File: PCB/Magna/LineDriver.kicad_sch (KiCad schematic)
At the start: 38 parts, among them J1301 PSG01550, U1301 NE5532, U1302 NE5532, U1303 NE5532

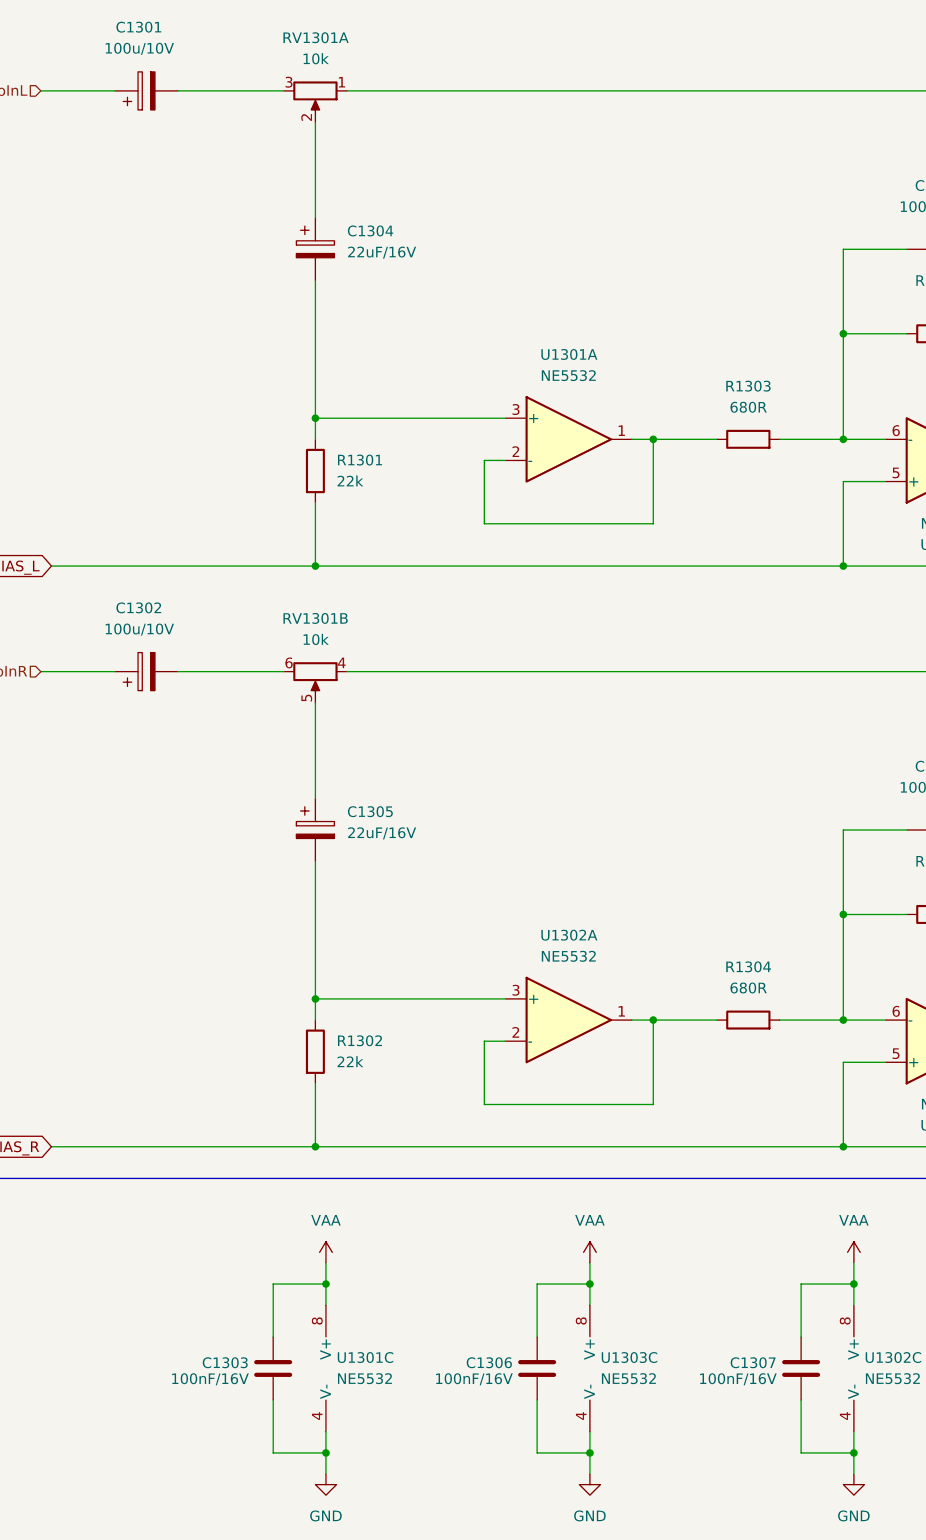
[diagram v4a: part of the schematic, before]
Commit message: Add even more component footprints and partnumbers
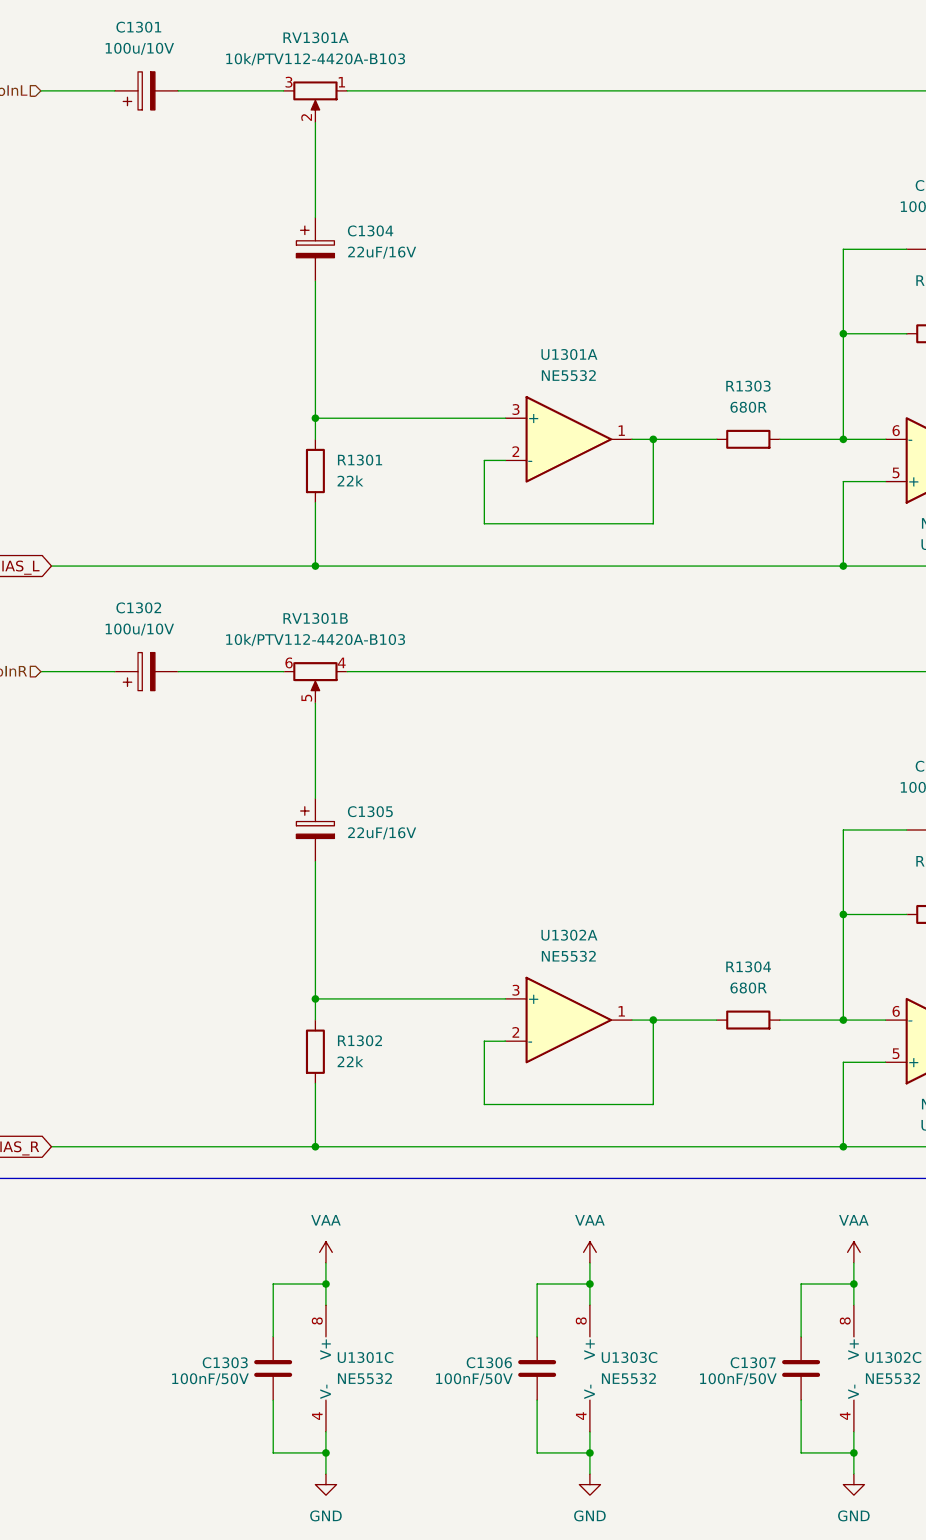
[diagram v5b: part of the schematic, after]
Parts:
- C1303, C1306, C1307: value 100nF/16V -> 100nF/50V; footprint Capacitor_SMD:C_0805_2012Metric -> Capacitor_SMD:C_0805_2012Metric_Pad1.18x1.45mm_HandSolder; LCSC C218638 -> C49678
- C1308, C1309, C1312, C1313: footprint Capacitor_SMD:C_0805_2012Metric -> Capacitor_SMD:C_0805_2012Metric_Pad1.18x1.45mm_HandSolder
- J1301: footprint (none) -> Skrooter_footprints:psg01550
- R1301, R1302, R1307, R1308, R1317, R1318: footprint Resistor_SMD:R_0805_2012Metric -> Resistor_SMD:R_0805_2012Metric_Pad1.20x1.40mm_HandSolder
- RV1301: value 10k -> 10k/PTV112-4420A-B103; footprint (none) -> Skrooter_footprints:Potentiometer_Bourns_PTV09A-1_Dual_Vertical
- U1301, U1302, U1303: footprint (none) -> Package_SO:SOIC-8_3.9x4.9mm_P1.27mm
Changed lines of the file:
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@@
       (effects (font (size 1.27 1.27)))
     )
-    (property "Value" "10k" (at 58.42 20.32 90)
-      (effects (font (size 1.27 1.27)))
-    )
-    (property "Footprint" "" (at 58.42 24.13 0)
+    (property "Value" "10k/PTV112-4420A-B103" (at 58.42 20.32 90)
+      (effects (font (size 1.27 1.27)))
+    )
+    (property "Footprint" "Skrooter_footprints:Potentiometer_Bourns_PTV09A-1_Dual_Vertical" (at 58.42 24.13 0)
       (effects (font (size 1.27 1.27)) hide)
     )
@@
       (effects (font (size 1.27 1.27)))
     )
-    (property "Footprint" "" (at 200.66 115.57 0)
+    (property "Footprint" "Package_SO:SOIC-8_3.9x4.9mm_P1.27mm" (at 200.66 115.57 0)
       (effects (font (size 1.27 1.27)) hide)
     )
@@
       (effects (font (size 1.27 1.27)) (justify left))
     )
-    (property "Value" "100nF/16V" (at 82.169 179.0773 0)
-      (effects (font (size 1.27 1.27)) (justify left))
-    )
-    (property "Footprint" "Capacitor_SMD:C_0805_2012Metric" (at 84.1248 181.61 0)
+    (property "Value" "100nF/50V" (at 82.169 179.0773 0)
+      (effects (font (size 1.27 1.27)) (justify left))
+    )
+    (property "Footprint" "Capacitor_SMD:C_0805_2012Metric_Pad1.18x1.45mm_HandSolder" (at 84.1248 181.61 0)
       (effects (font (size 1.27 1.27)) hide)
     )
@@
       (effects (font (size 1.27 1.27)) hide)
     )
-    (property "LCSC" "C218638" (at 85.09 177.8 0)
+    (property "LCSC" "C49678" (at 85.09 177.8 0)
       (effects (font (size 1.27 1.27)) hide)
     )
@@
       (effects (font (size 1.27 1.27)))
     )
-    (property "Footprint" "" (at 134.62 68.58 0)
+    (property "Footprint" "Package_SO:SOIC-8_3.9x4.9mm_P1.27mm" (at 134.62 68.58 0)
       (effects (font (size 1.27 1.27)) hide)
     )
@@
       (effects (font (size 1.27 1.27)))
     )
-    (property "Footprint" "" (at 200.66 45.72 0)
+    (property "Footprint" "Package_SO:SOIC-8_3.9x4.9mm_P1.27mm" (at 200.66 45.72 0)
       (effects (font (size 1.27 1.27)) hide)
     )
@@
       (effects (font (size 1.27 1.27)) (justify left))
     )
-    (property "Footprint" "" (at 265.43 91.44 0)
+    (property "Footprint" "Skrooter_footprints:psg01550" (at 265.43 91.44 0)
       (effects (font (size 1.27 1.27)) hide)
     )
@@
       (effects (font (size 1.27 1.27)))
     )
-    (property "Footprint" "Capacitor_SMD:C_0805_2012Metric" (at 137.16 42.2148 0)
+    (property "Footprint" "Capacitor_SMD:C_0805_2012Metric_Pad1.18x1.45mm_HandSolder" (at 137.16 42.2148 0)
       (effects (font (size 1.27 1.27)) hide)
     )
@@
       (effects (font (size 1.27 1.27)) (justify left))
     )
-    (property "Footprint" "Resistor_SMD:R_0805_2012Metric" (at 163.322 74.93 90)
+    (property "Footprint" "Resistor_SMD:R_0805_2012Metric_Pad1.20x1.40mm_HandSolder" (at 163.322 74.93 90)
       (effects (font (size 1.27 1.27)) hide)
     )
@@
       (effects (font (size 1.27 1.27)) (justify left))
     )
-    (property "Footprint" "Resistor_SMD:R_0805_2012Metric" (at 56.642 139.7 90)
+    (property "Footprint" "Resistor_SMD:R_0805_2012Metric_Pad1.20x1.40mm_HandSolder" (at 56.642 139.7 90)
       (effects (font (size 1.27 1.27)) hide)
     )
@@
       (effects (font (size 1.27 1.27)))
     )
-    (property "Footprint" "" (at 134.62 138.43 0)
+    (property "Footprint" "Package_SO:SOIC-8_3.9x4.9mm_P1.27mm" (at 134.62 138.43 0)
       (effects (font (size 1.27 1.27)) hide)
     )
@@
       (effects (font (size 1.27 1.27)) (justify left))
     )
-    (property "Footprint" "Resistor_SMD:R_0805_2012Metric" (at 247.142 124.46 90)
+    (property "Footprint" "Resistor_SMD:R_0805_2012Metric_Pad1.20x1.40mm_HandSolder" (at 247.142 124.46 90)
       (effects (font (size 1.27 1.27)) hide)
     )
@@
       (effects (font (size 1.27 1.27)))
     )
-    (property "Footprint" "" (at 88.9 135.89 0)
+    (property "Footprint" "Package_SO:SOIC-8_3.9x4.9mm_P1.27mm" (at 88.9 135.89 0)
       (effects (font (size 1.27 1.27)) hide)
     )
@@
       (effects (font (size 1.27 1.27)))
     )
-    (property "Footprint" "Capacitor_SMD:C_0805_2012Metric" (at 137.16 112.0648 0)
+    (property "Footprint" "Capacitor_SMD:C_0805_2012Metric_Pad1.18x1.45mm_HandSolder" (at 137.16 112.0648 0)
       (effects (font (size 1.27 1.27)) hide)
     )
@@
       (effects (font (size 1.27 1.27)) (justify left))
     )
-    (property "Footprint" "" (at 62.23 177.8 0)
+    (property "Footprint" "Package_SO:SOIC-8_3.9x4.9mm_P1.27mm" (at 62.23 177.8 0)
       (effects (font (size 1.27 1.27)) hide)
     )
@@
       (effects (font (size 1.27 1.27)) (justify left))
     )
-    (property "Footprint" "Resistor_SMD:R_0805_2012Metric" (at 247.142 54.61 90)
+    (property "Footprint" "Resistor_SMD:R_0805_2012Metric_Pad1.20x1.40mm_HandSolder" (at 247.142 54.61 90)
       (effects (font (size 1.27 1.27)) hide)
     )
@@
       (effects (font (size 1.27 1.27)))
     )
-    (property "Footprint" "Capacitor_SMD:C_0805_2012Metric" (at 204.47 34.5948 0)
+    (property "Footprint" "Capacitor_SMD:C_0805_2012Metric_Pad1.18x1.45mm_HandSolder" (at 204.47 34.5948 0)
       (effects (font (size 1.27 1.27)) hide)
     )
@@
       (effects (font (size 1.27 1.27)) (justify left))
     )
-    (property "Footprint" "" (at 125.73 177.8 0)
+    (property "Footprint" "Package_SO:SOIC-8_3.9x4.9mm_P1.27mm" (at 125.73 177.8 0)
       (effects (font (size 1.27 1.27)) hide)
     )
@@
       (effects (font (size 1.27 1.27)) (justify left))
     )
-    (property "Footprint" "Resistor_SMD:R_0805_2012Metric" (at 56.642 69.85 90)
+    (property "Footprint" "Resistor_SMD:R_0805_2012Metric_Pad1.20x1.40mm_HandSolder" (at 56.642 69.85 90)
       (effects (font (size 1.27 1.27)) hide)
     )
@@
       (effects (font (size 1.27 1.27)) (justify left))
     )
-    (property "Footprint" "" (at 93.98 177.8 0)
+    (property "Footprint" "Package_SO:SOIC-8_3.9x4.9mm_P1.27mm" (at 93.98 177.8 0)
       (effects (font (size 1.27 1.27)) hide)
     )
@@
       (effects (font (size 1.27 1.27)) (justify left))
     )
-    (property "Value" "100nF/16V" (at 50.419 179.0773 0)
-      (effects (font (size 1.27 1.27)) (justify left))
-    )
-    (property "Footprint" "Capacitor_SMD:C_0805_2012Metric" (at 52.3748 181.61 0)
+    (property "Value" "100nF/50V" (at 50.419 179.0773 0)
+      (effects (font (size 1.27 1.27)) (justify left))
+    )
+    (property "Footprint" "Capacitor_SMD:C_0805_2012Metric_Pad1.18x1.45mm_HandSolder" (at 52.3748 181.61 0)
       (effects (font (size 1.27 1.27)) hide)
     )
@@
       (effects (font (size 1.27 1.27)) hide)
     )
-    (property "LCSC" "C218638" (at 53.34 177.8 0)
+    (property "LCSC" "C49678" (at 53.34 177.8 0)
       (effects (font (size 1.27 1.27)) hide)
     )
@@
       (effects (font (size 1.27 1.27)))
     )
-    (property "Value" "10k" (at 58.42 90.17 90)
-      (effects (font (size 1.27 1.27)))
-    )
-    (property "Footprint" "" (at 58.42 93.98 0)
+    (property "Value" "10k/PTV112-4420A-B103" (at 58.42 90.17 90)
+      (effects (font (size 1.27 1.27)))
+    )
+    (property "Footprint" "Skrooter_footprints:Potentiometer_Bourns_PTV09A-1_Dual_Vertical" (at 58.42 93.98 0)
       (effects (font (size 1.27 1.27)) hide)
     )
@@
       (effects (font (size 1.27 1.27)))
     )
-    (property "Footprint" "" (at 88.9 66.04 0)
+    (property "Footprint" "Package_SO:SOIC-8_3.9x4.9mm_P1.27mm" (at 88.9 66.04 0)
       (effects (font (size 1.27 1.27)) hide)
     )
@@
       (effects (font (size 1.27 1.27)) (justify left))
     )
-    (property "Footprint" "Resistor_SMD:R_0805_2012Metric" (at 163.322 144.78 90)
+    (property "Footprint" "Resistor_SMD:R_0805_2012Metric_Pad1.20x1.40mm_HandSolder" (at 163.322 144.78 90)
       (effects (font (size 1.27 1.27)) hide)
     )
@@
       (effects (font (size 1.27 1.27)) (justify left))
     )
-    (property "Value" "100nF/16V" (at 113.919 179.0773 0)
-      (effects (font (size 1.27 1.27)) (justify left))
-    )
-    (property "Footprint" "Capacitor_SMD:C_0805_2012Metric" (at 115.8748 181.61 0)
+    (property "Value" "100nF/50V" (at 113.919 179.0773 0)
+      (effects (font (size 1.27 1.27)) (justify left))
+    )
+    (property "Footprint" "Capacitor_SMD:C_0805_2012Metric_Pad1.18x1.45mm_HandSolder" (at 115.8748 181.61 0)
       (effects (font (size 1.27 1.27)) hide)
     )
@@
       (effects (font (size 1.27 1.27)) hide)
     )
-    (property "LCSC" "C218638" (at 116.84 177.8 0)
+    (property "LCSC" "C49678" (at 116.84 177.8 0)
       (effects (font (size 1.27 1.27)) hide)
     )
@@
       (effects (font (size 1.27 1.27)))
     )
-    (property "Footprint" "Capacitor_SMD:C_0805_2012Metric" (at 204.47 104.4448 0)
-      (effects (font (size 1.27 1.27)) hide)
-    )
+    (property "Footprint" "Capacitor_SMD:C_0805_2012Metric_Pad1.18x1.45mm_HandSolder" (at 204.47 104.4448 0)
+      (effects (font (size 1.27 1.27)) hide)
+    )
